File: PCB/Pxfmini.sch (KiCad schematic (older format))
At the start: 9 parts, among them P0 Raspberry pi GPIO, P1 MPU9250, P2 MS5611, P3 PCA9685, P4 PCA9685_2, P5 UART, P6 RC INPUT

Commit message: 
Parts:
- added D1: LED_ARM, LEDs:LED-3MM, symbol LED
- added D2: LED_CALIBRATION, LEDs:LED-3MM, symbol LED
- added D3: LED_GPS, LEDs:LED-3MM, symbol LED
- added R3, R4, R5: 220, Resistors_ThroughHole:Resistor_Horizontal_RM7mm, symbol R
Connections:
- net +3V3: now also D1.2 (A), D2.2 (A), D3.2 (A)
- net CS_BARO: now also P0.24 (P24); no longer P0.22 (P22)
- net CS_MPU: now also P0.26 (P26); no longer P0.24 (P24)
- net GND: now also P0.20 (P20), P0.25 (P25), P0.39 (P39)
- net LED_ARM: now reaches P0.18 (P18)
- net LED_ARM: now also R3.2
- net LED_GPS: now reaches P0.36 (P36)
- net LED_GPS: now also R5.2
- new net: D1.1 (K), R3.1
- new net: D2.1 (K), R4.1
- new net: D3.1 (K), R5.1
- new net LED_CALIBRATION: P0.22 (P22), R4.2
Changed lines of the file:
@@
 P 2250 2300
 F 0 "P0" H 2250 3350 50  0000 C CNN
-F 1 "Raspberry pi GPIO" H 2650 2400 50  0000 L CNN
+F 1 "Raspberry pi GPIO" H 2600 2750 50  0000 L CNN
 F 2 "Pin_Headers:Pin_Header_Straight_2x20" H 2250 1350 50  0001 C CNN
 F 3 "" H 2250 1350 50  0000 C CNN
@@
 L GND #PWR07
 U 1 1 57EE81C1
-P 2800 1500
-F 0 "#PWR07" H 2800 1250 50  0001 C CNN
-F 1 "GND" H 2800 1350 50  0000 C CNN
-F 2 "" H 2800 1500 50  0000 C CNN
-F 3 "" H 2800 1500 50  0000 C CNN
-	1    2800 1500
+P 2800 1550
+F 0 "#PWR07" H 2800 1300 50  0001 C CNN
+F 1 "GND" H 2800 1400 50  0000 C CNN
+F 2 "" H 2800 1550 50  0000 C CNN
+F 3 "" H 2800 1550 50  0000 C CNN
+	1    2800 1550
 	1    0    0    -1
 $EndComp
@@
 Text Label 1650 2450 0    60   ~ 0
 SCLK
-Text Label 2650 2350 0    60   ~ 0
+Text Label 2700 2450 0    60   ~ 0
 CS_BARO
-Text Label 2650 2450 0    60   ~ 0
+Text Label 2700 2550 0    60   ~ 0
 CS_MPU
 $Comp
@@
 Connection ~ 2600 1350
 Wire Wire Line
-	2500 1550 2700 1550
-Wire Wire Line
-	2700 1550 2700 1500
-Wire Wire Line
-	2700 1500 2800 1500
+	2500 1550 2800 1550
 Wire Wire Line
 	2000 1750 1200 1750
@@
 Wire Wire Line
 	1650 2450 2000 2450
-Wire Wire Line
-	2500 2450 2650 2450
-Wire Wire Line
-	2500 2350 2650 2350
 Wire Wire Line
 	2500 1750 2550 1750
@@
 Wire Notes Line
 	9100 950  7700 950
+$Comp
+L GND #PWR017
+U 1 1 57EE3BBC
+P 1600 2550
+F 0 "#PWR017" H 1600 2300 50  0001 C CNN
+F 1 "GND" H 1600 2400 50  0000 C CNN
+F 2 "" H 1600 2550 50  0000 C CNN
+F 3 "" H 1600 2550 50  0000 C CNN
+	1    1600 2550
+	1    0    0    -1
+$EndComp
+$Comp
+L GND #PWR018
+U 1 1 57EE3BE2
+P 1600 3250
+F 0 "#PWR018" H 1600 3000 50  0001 C CNN
+F 1 "GND" H 1600 3100 50  0000 C CNN
+F 2 "" H 1600 3250 50  0000 C CNN
+F 3 "" H 1600 3250 50  0000 C CNN
+	1    1600 3250
+	1    0    0    -1
+$EndComp
+Wire Wire Line
+	1600 2550 2000 2550
+Wire Wire Line
+	1600 3250 2000 3250
+Wire Wire Line
+	2500 2450 2700 2450
+Wire Wire Line
+	2500 2550 2700 2550
+Text Label 2700 2150 0    60   ~ 0
+LED_ARM
+Text Label 2700 2350 0    60   ~ 0
+LED_CALIBRATION
+$Comp
+L GND #PWR019
+U 1 1 57EE400C
+P 3400 2050
+F 0 "#PWR019" H 3400 1800 50  0001 C CNN
+F 1 "GND" H 3400 1900 50  0000 C CNN
+F 2 "" H 3400 2050 50  0000 C CNN
+F 3 "" H 3400 2050 50  0000 C CNN
+	1    3400 2050
+	1    0    0    -1
+$EndComp
+Wire Wire Line
+	2500 2250 3250 2250
+Wire Wire Line
+	2500 2350 2700 2350
+Wire Wire Line
+	2500 2150 2700 2150
+Text Label 2750 3050 0    60   ~ 0
+LED_GPS
+Wire Wire Line
+	3250 2250 3250 2050
+Wire Wire Line
+	3250 2050 3400 2050
+Wire Wire Line
+	2500 3050 2750 3050
+$Comp
+L LED D1
+U 1 1 57EE4C97
+P 6750 4300
+F 0 "D1" H 6750 4400 50  0000 C CNN
+F 1 "LED_ARM" H 6750 4200 50  0000 C CNN
+F 2 "LEDs:LED-3MM" H 6750 4300 50  0001 C CNN
+F 3 "" H 6750 4300 50  0000 C CNN
+	1    6750 4300
+	1    0    0    -1
+$EndComp
+$Comp
+L LED D2
+U 1 1 57EE4CDA
+P 6750 4600
+F 0 "D2" H 6750 4700 50  0000 C CNN
+F 1 "LED_CALIBRATION" H 6900 4500 50  0000 C CNN
+F 2 "LEDs:LED-3MM" H 6750 4600 50  0001 C CNN
+F 3 "" H 6750 4600 50  0000 C CNN
+	1    6750 4600
+	1    0    0    -1
+$EndComp
+$Comp
+L LED D3
+U 1 1 57EE4D0F
+P 6750 4900
+F 0 "D3" H 6750 5000 50  0000 C CNN
+F 1 "LED_GPS" H 6750 4800 50  0000 C CNN
+F 2 "LEDs:LED-3MM" H 6750 4900 50  0001 C CNN
+F 3 "" H 6750 4900 50  0000 C CNN
+	1    6750 4900
+	1    0    0    -1
+$EndComp
+$Comp
+L +3.3V #PWR020
+U 1 1 57EE53C7
+P 6950 4150
+F 0 "#PWR020" H 6950 4000 50  0001 C CNN
+F 1 "+3.3V" H 6950 4290 50  0000 C CNN
+F 2 "" H 6950 4150 50  0000 C CNN
+F 3 "" H 6950 4150 50  0000 C CNN
+	1    6950 4150
+	1    0    0    -1
+$EndComp
+Wire Wire Line
+	6950 4150 6950 4900
+Connection ~ 6950 4300
+Connection ~ 6950 4600
+$Comp
+L R R3
+U 1 1 57EE5467
+P 6400 4300
+F 0 "R3" V 6480 4300 50  0000 C CNN
+F 1 "220" V 6400 4300 50  0000 C CNN
+F 2 "Resistors_ThroughHole:Resistor_Horizontal_RM7mm" V 6330 4300 50  0001 C CNN
+F 3 "" H 6400 4300 50  0000 C CNN
+	1    6400 4300
+	0    1    1    0
+$EndComp
+$Comp
+L R R4
+U 1 1 57EE55DD
+P 6400 4600
+F 0 "R4" V 6480 4600 50  0000 C CNN
+F 1 "220" V 6400 4600 50  0000 C CNN
+F 2 "Resistors_ThroughHole:Resistor_Horizontal_RM7mm" V 6330 4600 50  0001 C CNN
+F 3 "" H 6400 4600 50  0000 C CNN
+	1    6400 4600
+	0    1    1    0
+$EndComp
+$Comp
+L R R5
+U 1 1 57EE5673
+P 6400 4900
+F 0 "R5" V 6480 4900 50  0000 C CNN
+F 1 "220" V 6400 4900 50  0000 C CNN
+F 2 "Resistors_ThroughHole:Resistor_Horizontal_RM7mm" V 6330 4900 50  0001 C CNN
+F 3 "" H 6400 4900 50  0000 C CNN
+	1    6400 4900
+	0    1    1    0
+$EndComp
+Text Label 5850 4300 0    60   ~ 0
+LED_ARM
+Wire Wire Line
+	5850 4300 6250 4300
+Text Label 5500 4600 0    60   ~ 0
+LED_CALIBRATION
+Text Label 5850 4900 0    60   ~ 0
+LED_GPS
+Wire Wire Line
+	5500 4600 6250 4600
+Wire Wire Line
+	5850 4900 6250 4900
 $EndSCHEMATC

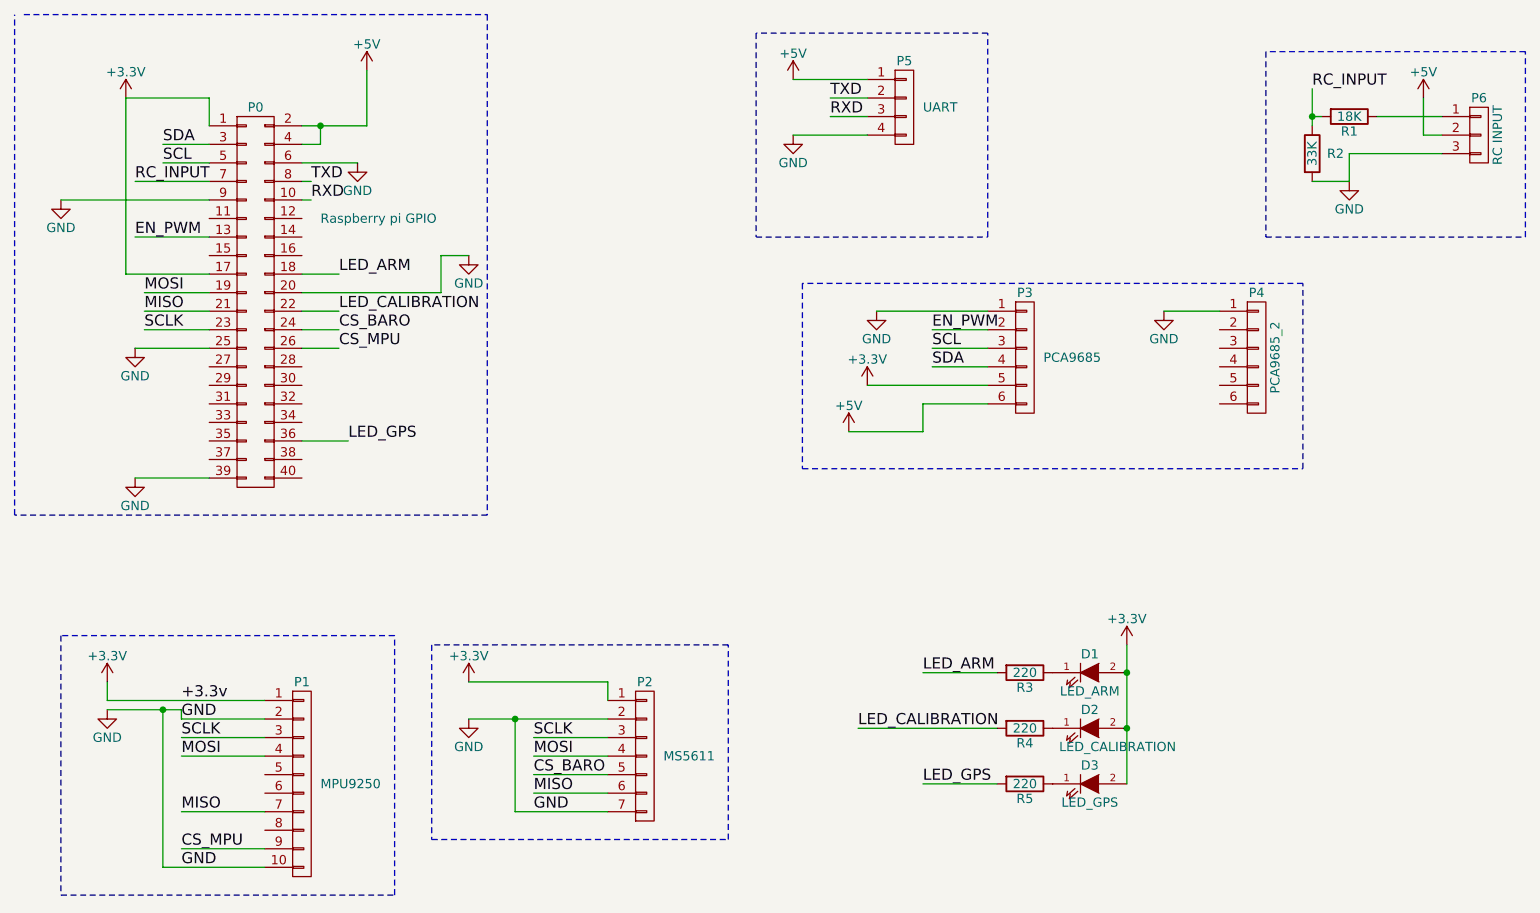
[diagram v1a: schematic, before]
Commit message: 
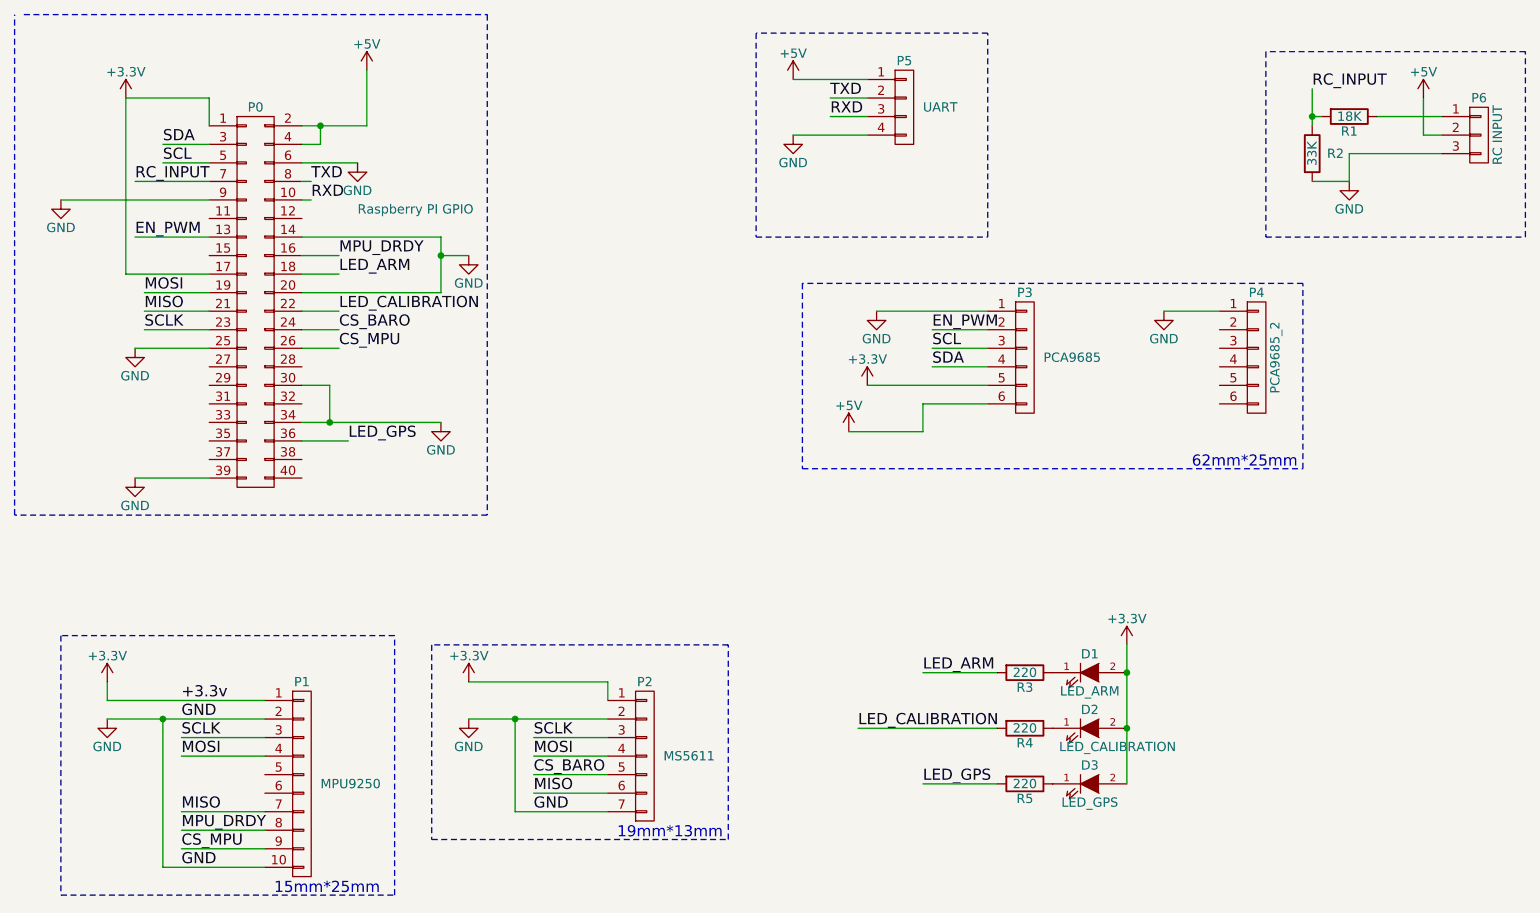
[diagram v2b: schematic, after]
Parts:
- P0: value Raspberry pi GPIO -> Raspberry PI GPIO
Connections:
- net GND: now also P0.14 (P14), P0.30 (P30), P0.34 (P34)
- net MPU_DRDY: now reaches P1.8 (P8)
- net MPU_DRDY: now also P0.16 (P16)
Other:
- note added: "15mm*25mm"
- note added: "19mm*13mm"
- note added: "62mm*25mm"
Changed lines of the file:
@@
 Rev ""
 Comp ""
-Comment1 ""
+Comment1 "hat dimension:65mm*56mm"
 Comment2 ""
 Comment3 ""
@@
 Text Label 1850 4450 0    60   ~ 0
 +3.3v
-Text Label 1850 4550 0    60   ~ 0
-GND
 $Comp
 L GND #PWR01
 U 1 1 57EE7200
-P 1450 4500
-F 0 "#PWR01" H 1450 4250 50  0001 C CNN
-F 1 "GND" H 1450 4350 50  0000 C CNN
-F 2 "" H 1450 4500 50  0000 C CNN
-F 3 "" H 1450 4500 50  0000 C CNN
-	1    1450 4500
+P 1450 4550
+F 0 "#PWR01" H 1450 4300 50  0001 C CNN
+F 1 "GND" H 1450 4400 50  0000 C CNN
+F 2 "" H 1450 4550 50  0000 C CNN
+F 3 "" H 1450 4550 50  0000 C CNN
+	1    1450 4550
 	1    0    0    -1
 $EndComp
@@
 P 2250 2300
 F 0 "P0" H 2250 3350 50  0000 C CNN
-F 1 "Raspberry pi GPIO" H 2600 2750 50  0000 L CNN
+F 1 "Raspberry PI GPIO" H 2800 2800 50  0000 L CNN
 F 2 "Pin_Headers:Pin_Header_Straight_2x20" H 2250 1350 50  0001 C CNN
 F 3 "" H 2250 1350 50  0000 C CNN
@@
 	1450 4450 2300 4450
 Wire Wire Line
-	1850 4550 2300 4550
-Wire Wire Line
-	1450 4500 1850 4500
-Wire Wire Line
-	1850 4500 1850 4550
-Wire Wire Line
 	1450 4350 1450 4450
 Wire Wire Line
@@
 Wire Wire Line
 	1750 5350 2300 5350
-Wire Wire Line
-	1750 4500 1750 5350
-Connection ~ 1750 4500
 Wire Wire Line
 	1550 1200 2000 1200
@@
 $EndComp
 Wire Wire Line
-	2500 2250 3250 2250
+	3250 2250 2500 2250
 Wire Wire Line
 	2500 2350 2700 2350
@@
 LED_GPS
 Wire Wire Line
-	3250 2250 3250 2050
+	3250 1950 3250 2250
 Wire Wire Line
 	3250 2050 3400 2050
@@
 Wire Wire Line
 	5850 4900 6250 4900
+Text Notes 2350 5500 0    60   ~ 0
+15mm*25mm
+Text Notes 4200 5200 0    60   ~ 0
+19mm*13mm
+Text Notes 7300 3200 0    60   ~ 0
+62mm*25mm
+Wire Wire Line
+	1450 4550 2300 4550
+Wire Wire Line
+	1750 5350 1750 4550
+Connection ~ 1750 4550
+Text Label 1850 5150 0    60   ~ 0
+MPU_DRDY
+Wire Wire Line
+	1850 5150 2300 5150
+Text Label 1850 4550 0    60   ~ 0
+GND
+Text Label 2700 2050 0    60   ~ 0
+MPU_DRDY
+Wire Wire Line
+	2500 1950 3250 1950
+Connection ~ 3250 2050
+Wire Wire Line
+	2500 2050 2700 2050
+$Comp
+L GND #PWR021
+U 1 1 57F96D5B
+P 3250 2950
+F 0 "#PWR021" H 3250 2700 50  0001 C CNN
+F 1 "GND" H 3250 2800 50  0000 C CNN
+F 2 "" H 3250 2950 50  0000 C CNN
+F 3 "" H 3250 2950 50  0000 C CNN
+	1    3250 2950
+	1    0    0    -1
+$EndComp
+Wire Wire Line
+	2500 2950 3250 2950
+Wire Wire Line
+	2500 2750 2650 2750
+Wire Wire Line
+	2650 2750 2650 2950
+Connection ~ 2650 2950
 $EndSCHEMATC

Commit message: 
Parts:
- removed P4: PCA9685_2, Pin_Headers:Pin_Header_Straight_1x06, symbol CONN_01X06
- P1: footprint Pin_Headers:Pin_Header_Straight_1x10 -> Raspmini:MPU9250
- P2: footprint Pin_Headers:Pin_Header_Straight_1x07 -> Raspmini:MS5611
- P3: footprint Pin_Headers:Pin_Header_Straight_1x06 -> Raspmini:PCA9685
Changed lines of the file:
@@
 F 0 "P1" H 2500 5450 50  0000 C CNN
 F 1 "MPU9250" H 2600 4900 50  0000 L CNN
-F 2 "Pin_Headers:Pin_Header_Straight_1x10" H 2500 4900 50  0001 C CNN
+F 2 "Raspmini:MPU9250" H 2500 4900 50  0001 C CNN
 F 3 "" H 2500 4900 50  0000 C CNN
 	1    2500 4900
@@
 F 0 "P2" H 4350 5150 50  0000 C CNN
 F 1 "MS5611" H 4450 4750 50  0000 L CNN
-F 2 "Pin_Headers:Pin_Header_Straight_1x07" H 4350 4750 50  0001 C CNN
+F 2 "Raspmini:MS5611" H 4350 4750 50  0001 C CNN
 F 3 "" H 4350 4750 50  0000 C CNN
 	1    4350 4750
@@
 P 2250 2300
 F 0 "P0" H 2250 3350 50  0000 C CNN
-F 1 "Raspberry PI GPIO" H 2800 2800 50  0000 L CNN
+F 1 "Raspberry PI GPIO" H 1100 3750 50  0000 L CNN
 F 2 "Pin_Headers:Pin_Header_Straight_2x20" H 2250 1350 50  0001 C CNN
 F 3 "" H 2250 1350 50  0000 C CNN
@@
 L +3.3V #PWR05
 U 1 1 57EE8040
-P 1550 1200
-F 0 "#PWR05" H 1550 1050 50  0001 C CNN
-F 1 "+3.3V" H 1550 1340 50  0000 C CNN
-F 2 "" H 1550 1200 50  0000 C CNN
-F 3 "" H 1550 1200 50  0000 C CNN
-	1    1550 1200
+P 1450 1350
+F 0 "#PWR05" H 1450 1200 50  0001 C CNN
+F 1 "+3.3V" H 1450 1490 50  0000 C CNN
+F 2 "" H 1450 1350 50  0000 C CNN
+F 3 "" H 1450 1350 50  0000 C CNN
+	1    1450 1350
 	1    0    0    -1
 $EndComp
@@
 F 0 "P3" H 6400 2950 50  0000 C CNN
 F 1 "PCA9685" H 6500 2600 50  0000 L CNN
-F 2 "Pin_Headers:Pin_Header_Straight_1x06" H 6400 2600 50  0001 C CNN
+F 2 "Raspmini:PCA9685" H 6400 2600 50  0001 C CNN
 F 3 "" H 6400 2600 50  0000 C CNN
 	1    6400 2600
@@
 	1750 5350 2300 5350
 Wire Wire Line
-	1550 1200 2000 1200
-Wire Wire Line
-	2000 1200 2000 1350
-Wire Wire Line
 	1750 1450 2000 1450
 Wire Wire Line
@@
 	1600 1950 2000 1950
 Wire Wire Line
-	2000 2150 1550 2150
-Wire Wire Line
-	1550 2150 1550 1200
+	1400 2150 2000 2150
 Wire Wire Line
 	1650 2250 2000 2250
@@
 Wire Wire Line
 	8150 1650 7950 1650
-$Comp
-L CONN_01X06 P4
-U 1 1 57EEAC6F
-P 7650 2600
-F 0 "P4" H 7650 2950 50  0000 C CNN
-F 1 "PCA9685_2" V 7750 2600 50  0000 C CNN
-F 2 "Pin_Headers:Pin_Header_Straight_1x06" H 7650 2600 50  0001 C CNN
-F 3 "" H 7650 2600 50  0000 C CNN
-	1    7650 2600
-	1    0    0    -1
-$EndComp
+Wire Notes Line
+	3200 4150 3200 5200
+Wire Notes Line
+	3200 5200 4800 5200
+Wire Notes Line
+	4800 5200 4800 4150
+Wire Notes Line
+	4800 4150 3200 4150
+Wire Notes Line
+	5200 2200 5200 3200
+Wire Notes Line
+	5200 3200 7900 3200
+Wire Notes Line
+	7900 3200 7900 2200
+Wire Notes Line
+	7900 2200 5200 2200
+Wire Notes Line
+	1200 4100 1200 5500
+Wire Notes Line
+	1200 5500 3000 5500
+Wire Notes Line
+	3000 5500 3000 4100
+Wire Notes Line
+	3000 4100 1200 4100
+Wire Notes Line
+	1000 750  3500 750
+Wire Notes Line
+	3500 750  3500 3450
+Wire Notes Line
+	3500 3450 950  3450
+Wire Notes Line
+	950  3450 950  750
+Wire Notes Line
+	4950 850  4950 1950
+Wire Notes Line
+	4950 1950 6200 1950
+Wire Notes Line
+	6200 1950 6200 850
+Wire Notes Line
+	6200 850  4950 850
+Wire Notes Line
+	7700 950  7700 1950
+Wire Notes Line
+	7700 1950 9100 1950
+Wire Notes Line
+	9100 1950 9100 950
+Wire Notes Line
+	9100 950  7700 950
 $Comp
 L GND #PWR016
-U 1 1 57EEAF4A
-P 7150 2350
-F 0 "#PWR016" H 7150 2100 50  0001 C CNN
-F 1 "GND" H 7150 2200 50  0000 C CNN
-F 2 "" H 7150 2350 50  0000 C CNN
-F 3 "" H 7150 2350 50  0000 C CNN
-	1    7150 2350
-	1    0    0    -1
-$EndComp
-Wire Wire Line
-	7150 2350 7450 2350
-Wire Notes Line
-	3200 4150 3200 5200
-Wire Notes Line
-	3200 5200 4800 5200
-Wire Notes Line
-	4800 5200 4800 4150
-Wire Notes Line
-	4800 4150 3200 4150
-Wire Notes Line
-	5200 2200 5200 3200
-Wire Notes Line
-	5200 3200 7900 3200
-Wire Notes Line
-	7900 3200 7900 2200
-Wire Notes Line
-	7900 2200 5200 2200
-Wire Notes Line
-	1200 4100 1200 5500
-Wire Notes Line
-	1200 5500 3000 5500
-Wire Notes Line
-	3000 5500 3000 4100
-Wire Notes Line
-	3000 4100 1200 4100
-Wire Notes Line
-	1000 750  3500 750
-Wire Notes Line
-	3500 750  3500 3450
-Wire Notes Line
-	3500 3450 950  3450
-Wire Notes Line
-	950  3450 950  750
-Wire Notes Line
-	4950 850  4950 1950
-Wire Notes Line
-	4950 1950 6200 1950
-Wire Notes Line
-	6200 1950 6200 850
-Wire Notes Line
-	6200 850  4950 850
-Wire Notes Line
-	7700 950  7700 1950
-Wire Notes Line
-	7700 1950 9100 1950
-Wire Notes Line
-	9100 1950 9100 950
-Wire Notes Line
-	9100 950  7700 950
-$Comp
-L GND #PWR017
 U 1 1 57EE3BBC
 P 1600 2550
-F 0 "#PWR017" H 1600 2300 50  0001 C CNN
+F 0 "#PWR016" H 1600 2300 50  0001 C CNN
 F 1 "GND" H 1600 2400 50  0000 C CNN
 F 2 "" H 1600 2550 50  0000 C CNN
@@
 $EndComp
 $Comp
-L GND #PWR018
+L GND #PWR017
 U 1 1 57EE3BE2
 P 1600 3250
-F 0 "#PWR018" H 1600 3000 50  0001 C CNN
+F 0 "#PWR017" H 1600 3000 50  0001 C CNN
 F 1 "GND" H 1600 3100 50  0000 C CNN
 F 2 "" H 1600 3250 50  0000 C CNN
@@
 LED_CALIBRATION
 $Comp
-L GND #PWR019
+L GND #PWR018
 U 1 1 57EE400C
 P 3400 2050
-F 0 "#PWR019" H 3400 1800 50  0001 C CNN
+F 0 "#PWR018" H 3400 1800 50  0001 C CNN
 F 1 "GND" H 3400 1900 50  0000 C CNN
 F 2 "" H 3400 2050 50  0000 C CNN
@@
 $EndComp
 $Comp
-L +3.3V #PWR020
+L +3.3V #PWR019
 U 1 1 57EE53C7
 P 6950 4150
-F 0 "#PWR020" H 6950 4000 50  0001 C CNN
+F 0 "#PWR019" H 6950 4000 50  0001 C CNN
 F 1 "+3.3V" H 6950 4290 50  0000 C CNN
 F 2 "" H 6950 4150 50  0000 C CNN
@@
 	2500 2050 2700 2050
 $Comp
-L GND #PWR021
+L GND #PWR020
 U 1 1 57F96D5B
 P 3250 2950
-F 0 "#PWR021" H 3250 2700 50  0001 C CNN
+F 0 "#PWR020" H 3250 2700 50  0001 C CNN
 F 1 "GND" H 3250 2800 50  0000 C CNN
 F 2 "" H 3250 2950 50  0000 C CNN
@@
 	2650 2750 2650 2950
 Connection ~ 2650 2950
+$Comp
+L +3.3V #PWR?
+U 1 1 57FCBC4B
+P 1400 2100
+F 0 "#PWR?" H 1400 1950 50  0001 C CNN
+F 1 "+3.3V" H 1400 2240 50  0000 C CNN
+F 2 "" H 1400 2100 50  0000 C CNN
+F 3 "" H 1400 2100 50  0000 C CNN
+	1    1400 2100
+	1    0    0    -1
+$EndComp
+Wire Wire Line
+	1400 2150 1400 2100
+Wire Wire Line
+	2000 1350 1450 1350
 $EndSCHEMATC

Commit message: 
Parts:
- R1, R2, R3, R4, R5: footprint Resistors_ThroughHole:Resistor_Horizontal_RM7mm -> Resistors_ThroughHole:Resistor_Horizontal_RM10mm
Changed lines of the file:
@@
 F 0 "R1" V 8230 1300 50  0000 C CNN
 F 1 "18K" V 8150 1300 50  0000 C CNN
-F 2 "Resistors_ThroughHole:Resistor_Horizontal_RM7mm" V 8080 1300 50  0001 C CNN
+F 2 "Resistors_ThroughHole:Resistor_Horizontal_RM10mm" V 8080 1300 50  0001 C CNN
 F 3 "" H 8150 1300 50  0000 C CNN
 	1    8150 1300
@@
 F 0 "R2" H 8030 1500 50  0000 L CNN
 F 1 "33K" V 7950 1500 50  0000 C CNN
-F 2 "Resistors_ThroughHole:Resistor_Horizontal_RM7mm" V 7880 1500 50  0001 C CNN
+F 2 "Resistors_ThroughHole:Resistor_Horizontal_RM10mm" V 7880 1500 50  0001 C CNN
 F 3 "" H 7950 1500 50  0000 C CNN
 	1    7950 1500
@@
 F 0 "R3" V 6480 4300 50  0000 C CNN
 F 1 "220" V 6400 4300 50  0000 C CNN
-F 2 "Resistors_ThroughHole:Resistor_Horizontal_RM7mm" V 6330 4300 50  0001 C CNN
+F 2 "Resistors_ThroughHole:Resistor_Horizontal_RM10mm" V 6330 4300 50  0001 C CNN
 F 3 "" H 6400 4300 50  0000 C CNN
 	1    6400 4300
@@
 F 0 "R4" V 6480 4600 50  0000 C CNN
 F 1 "220" V 6400 4600 50  0000 C CNN
-F 2 "Resistors_ThroughHole:Resistor_Horizontal_RM7mm" V 6330 4600 50  0001 C CNN
+F 2 "Resistors_ThroughHole:Resistor_Horizontal_RM10mm" V 6330 4600 50  0001 C CNN
 F 3 "" H 6400 4600 50  0000 C CNN
 	1    6400 4600
@@
 F 0 "R5" V 6480 4900 50  0000 C CNN
 F 1 "220" V 6400 4900 50  0000 C CNN
-F 2 "Resistors_ThroughHole:Resistor_Horizontal_RM7mm" V 6330 4900 50  0001 C CNN
+F 2 "Resistors_ThroughHole:Resistor_Horizontal_RM10mm" V 6330 4900 50  0001 C CNN
 F 3 "" H 6400 4900 50  0000 C CNN
 	1    6400 4900
